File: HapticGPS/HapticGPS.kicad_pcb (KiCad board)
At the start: 4 copper layers, 35 x 50 mm, 106 parts, among them IC1 BOS1921CQR, J2 PZ, J3 Conn_01x02, J4 Conn_01x02, J5 Conn_01x10, Q1 RU1J002, U1 NPM1300, U2 NRF54L15-QFAA-R, U3 DRV2667RGPR, U4 CY15B108, U5 LC29H, U6 LSM6, U7 TPS22917DBV, Y1 32MHz, Y2 32kHz

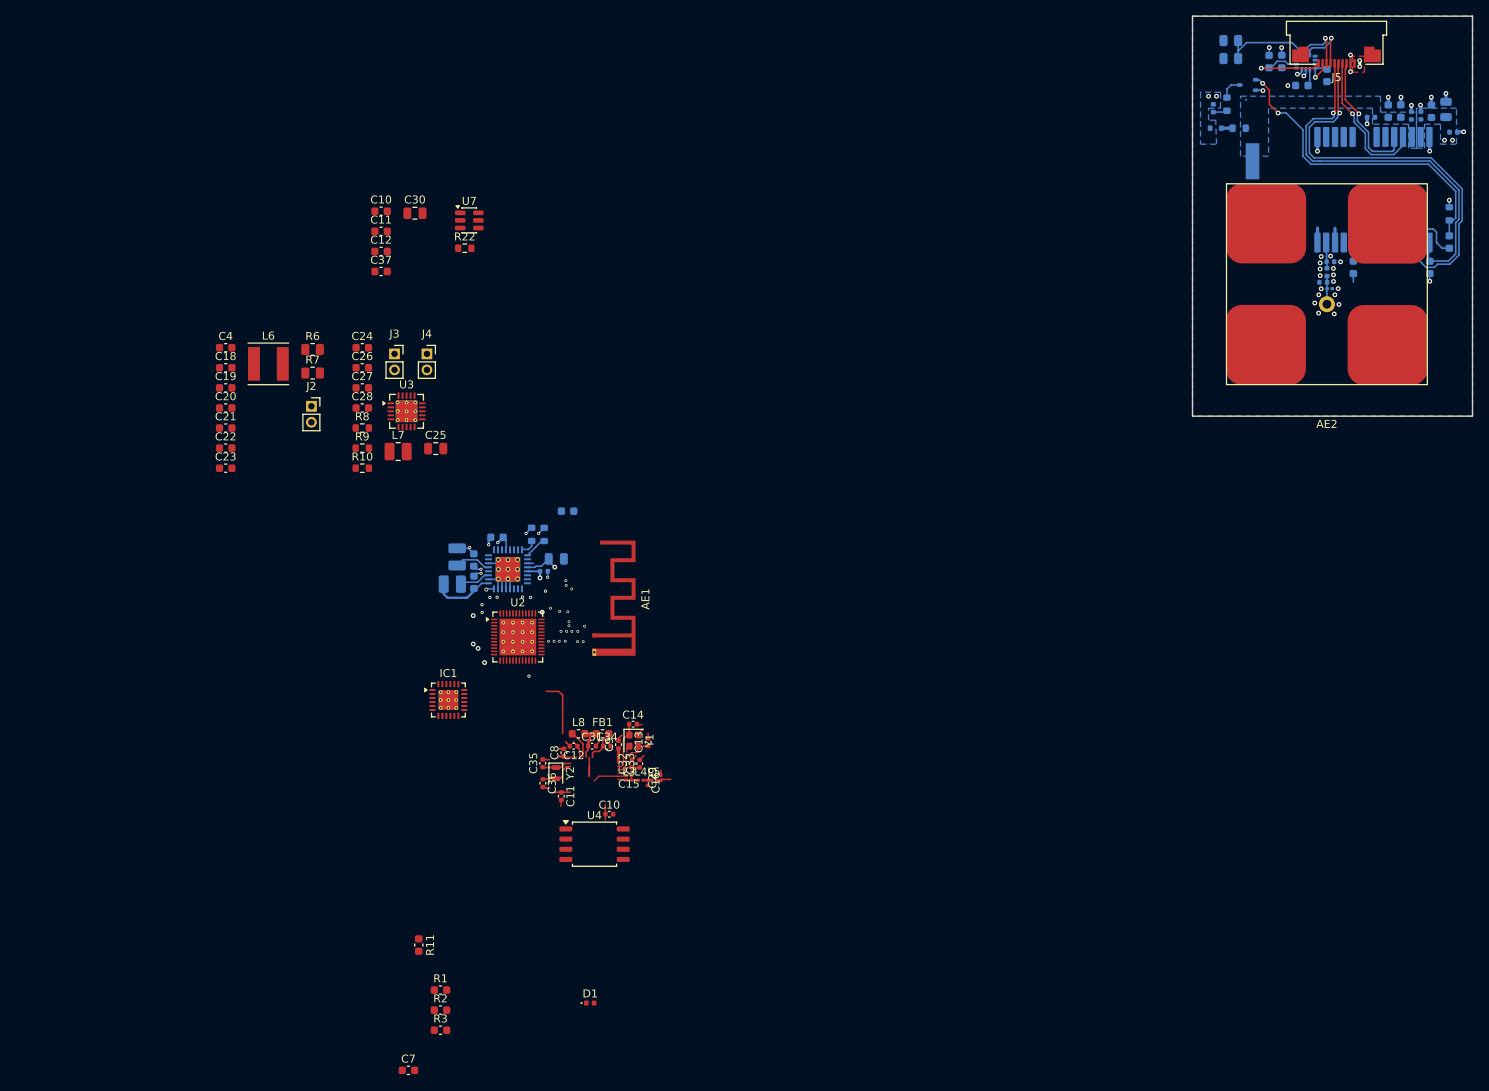
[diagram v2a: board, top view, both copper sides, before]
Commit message: eliminating GPS, and second piezo driver
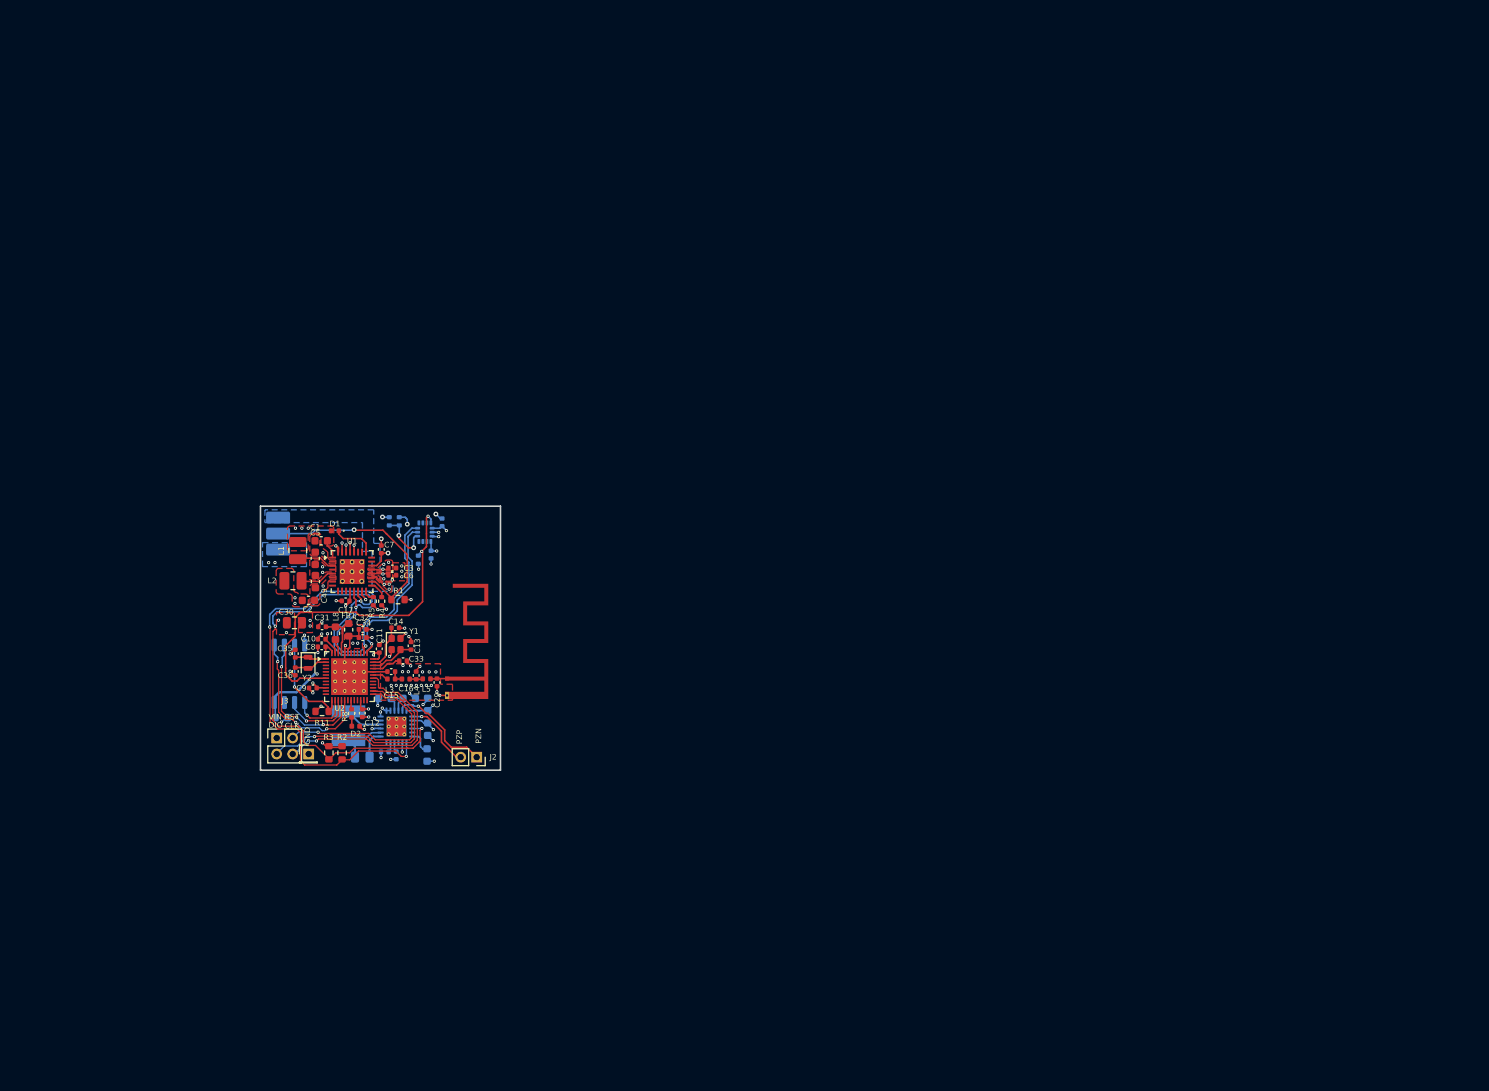
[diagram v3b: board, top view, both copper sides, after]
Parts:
- removed AE2: ANT-GNCP, Sadman_antenna:NT-GNCP-TH258L15
- removed the C10 at (174.1, 137.2)
- removed the C10 at (145.6, 61.9)
- removed the C11 at (145.6, 64.4)
- removed the C11 at (168.1, 135.0)
- removed the C12 at (169.7, 128.8)
- removed the C12 at (145.6, 66.9)
- removed C18, C27, C4, C42, C47, C48: 100nF, Capacitor_SMD:C_0603_1608Metric
- removed C24: 1uF, Capacitor_SMD:C_0603_1608Metric
- removed C25: 10uF, Capacitor_SMD:C_0805_2012Metric
- removed C40, C43: 33pF, Capacitor_SMD:C_0402_1005Metric
- removed C41: 4.7uF, Capacitor_SMD:C_0603_1608Metric
- removed C44: 220mF, sadman_power_passive:FC0H224ZFTBR24
- removed C45, C46: 2pF, Capacitor_SMD:C_0402_1005Metric
- removed D3: TVS, Diode_SMD:D_0402_1005Metric
- removed D4: 1N4148WT, Diode_SMD:D_SOD-523
- removed D5: TVS, Diode_SMD:D_0201_0603Metric
- removed D6: YELLOW, Diode_SMD:D_0402_1005Metric
- removed J5: Conn_01x10, Connector_FFC-FPC:Amphenol_F32Q-1A7x1-11010_1x10-1MP_P0.5mm_Horizontal
- removed L7: 2.2uF, Inductor_SMD:L_1008_2520Metric
- removed L9: 6nH, Inductor_SMD:L_0402_1005Metric
- removed Q1: RU1J002, Package_TO_SOT_SMD:SOT-323_SC-70
- removed R10: 7.68K, Resistor_SMD:R_0603_1608Metric
- removed R12, R22: 1k, Resistor_SMD:R_0603_1608Metric
- removed R13: 1, Resistor_SMD:R_0805_2012Metric
- removed R14, R17, R18, R20: 2.2k, Capacitor_SMD:C_0603_1608Metric
- removed R15: 100K, Resistor_SMD:R_0603_1608Metric
- removed R16: 75, Resistor_SMD:R_0603_1608Metric
- removed R9: 37k, Resistor_SMD:R_0603_1608Metric
- removed U3: DRV2667RGPR, Package_DFN_QFN:Texas_RGP0020D_VQFN-20-1EP_4x4mm_P0.5mm_EP2.7x2.7mm_ThermalVias
- removed U5: LC29H, Sadman_RF_receivers:LC29H
- removed U7: TPS22917DBV, Package_TO_SOT_SMD:SOT-23-6
- added C10: 100nF, Capacitor_SMD:C_0402_1005Metric, F.Cu at (138.1, 115.4)
- added C11: 100nF, Capacitor_SMD:C_0402_1005Metric, F.Cu at (145.3, 116.6)
- added C12: 100nF, Capacitor_SMD:C_0402_1005Metric, F.Cu at (143.2, 124.6)
- added C49: 10uF, Capacitor_SMD:C_0603_1608Metric, F.Cu at (137.4, 108.2)
- added J1: Conn_01x01, Connector_PinHeader_2.00mm:PinHeader_1x01_P2.00mm_Vertical, F.Cu at (136.5, 129.7)
- C1, C2, C3, U1: moved to F.Cu
- C15, C16, C29: footprint Capacitor_SMD:C_0201_0603Metric -> Capacitor_SMD:C_0402_1005Metric
- C17, C6: footprint Capacitor_SMD:C_0603_1608Metric -> Capacitor_SMD:C_0402_1005Metric; moved to F.Cu
- C19, C20, C21, C22, C23, C37, IC1, L6, R6, U4: moved to B.Cu
- C26, C28: footprint Capacitor_SMD:C_0603_1608Metric -> Capacitor_SMD:C_0402_1005Metric; moved to B.Cu
- C38: value 10uF -> 100nF; footprint Capacitor_SMD:C_0805_2012Metric -> Capacitor_SMD:C_0402_1005Metric
- C39, C7: footprint Capacitor_SMD:C_0603_1608Metric -> Capacitor_SMD:C_0402_1005Metric
- C5: footprint Capacitor_SMD:C_0805_2012Metric -> Capacitor_SMD:C_0603_1608Metric; moved to F.Cu
- D2: value TVS -> GREEN; footprint Diode_SMD:D_0402_1005Metric -> LED_SMD:LED_0402_1005Metric; moved to F.Cu
- J3: value Conn_01x02 -> Conn_02x02_Counter_Clockwise; footprint Connector_PinSocket_2.00mm:PinSocket_1x02_P2.00mm_Vertical -> Connector_PinHeader_2.00mm:PinHeader_2x02_P2.00mm_Vertical
- J4: value Conn_01x02 -> Conn_01x03; footprint Connector_PinSocket_2.00mm:PinSocket_1x02_P2.00mm_Vertical -> Solderpads:01x03_1.5x3; moved to B.Cu
- L1, L2: value 2.2uF -> 2.2uH; moved to F.Cu
- L3, L4, L5: footprint Inductor_SMD:L_0201_0603Metric -> Inductor_SMD:L_0402_1005Metric
- R1, R11, R2, R3: footprint Capacitor_SMD:C_0603_1608Metric -> Resistor_SMD:R_0603_1608Metric
- R19: footprint Resistor_SMD:R_0805_2012Metric -> Resistor_SMD:R_0402_1005Metric
- R21: value 2.2k -> 10k; footprint Capacitor_SMD:C_0603_1608Metric -> Resistor_SMD:R_0402_1005Metric
- R4: value 100K -> 300K; footprint Resistor_SMD:R_0603_1608Metric -> Resistor_SMD:R_0402_1005Metric; moved to F.Cu
- R5: value 100K -> 150K; footprint Resistor_SMD:R_0603_1608Metric -> Resistor_SMD:R_0402_1005Metric; moved to F.Cu
- R7: footprint Resistor_SMD:R_0805_2012Metric -> Resistor_SMD:R_0402_1005Metric; moved to B.Cu
- R8: value 510k -> 120; footprint Resistor_SMD:R_0603_1608Metric -> Resistor_SMD:R_0402_1005Metric
- Y2: value 32kHz -> 32.768kHz
- moved D2 156.0 mm to (142.4, 126.2), turned to 180 degrees
- moved C39 136.8 mm to (151.8, 104.8), turned to -90 degrees
- moved C38 135.7 mm to (153.2, 100.8)
- moved R21 128.7 mm to (150.2, 105.4)
- moved U6 124.8 mm to (151.0, 102.0), turned to -90 degrees
- moved R19 120.0 mm to (146.6, 100.6), turned to -90 degrees
- moved D1 67.1 mm to (139.8, 101.8), turned to 180 degrees
- moved C7 65.2 mm to (145.6, 104.2), turned to 90 degrees
- moved C37 57.1 mm to (133.1, 125.2)
- moved C30 53.4 mm to (134.7, 113.3), turned to 180 degrees
- moved C19 52.3 mm to (151.3, 129.8), turned to -90 degrees
- moved R6 51.3 mm to (143.2, 130.1)
- moved J3 50.2 mm to (132.5, 127.7)
- moved R1 49.1 mm to (147.7, 110.4)
- moved C26 48.6 mm to (147.5, 129.9), turned to -90 degrees
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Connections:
- net Net-(U1-PVDD) renamed /POWER/PVDD
- AE1 pad 2: (no net) -> GND
- C17 pad 1: +3VDC1 -> +3VDC2
- C22 pad 2: /PIEZOELECTRIC DRIVER/PZ_VDD_F -> +3VDC2
- C23 pad 2: /PIEZOELECTRIC DRIVER/PZ_VDD_F -> +3VDC2
- C26 pad 1: Net-(U3-VREG) -> Net-(IC1-REG)
- C28 pad 1: Net-(U3-VPUMP) -> Net-(IC1-PUMP)
- C37 pad 1: Net-(U4-VDD) -> +3VDC1
- C38 pad 1: /VINC_GPS -> +3VDC1
- C39 pad 1: /VINC_GPS -> +3VDC1
- D1 pad 2: GND -> +3VDC1
- D2 pad 1: /VINC_GPS -> GND
- D2 pad 2: GND -> Net-(D2-A)
- IC1 pad 2: /PIEZOELECTRIC DRIVER/PZ_VDD_F -> +3VDC2
- IC1 pad 24: /PIEZOELECTRIC DRIVER/PZ_VDD_F -> +3VDC2
- J3 pad 1: /PIEZOELECTRIC DRIVER 2/PZ2_OUT+ -> +5V
- J3 pad 2: /PIEZOELECTRIC DRIVER 2/PZ2_OUT- -> /CONTROLLER/NRF_RESET
- J4 pad 1: /PIEZOELECTRIC DRIVER 2/PZ2_IN+ -> GND
- J4 pad 2: /PIEZOELECTRIC DRIVER 2/PZ2_IN- -> /POWER/VBAT_NTC
- R2 pad 1: +2V8 -> +3VDC1
- R3 pad 1: +2V8 -> +3VDC1
- R7 pad 1: +3VDC2 -> +3VDC1
- R7 pad 2: /PIEZOELECTRIC DRIVER/PZ_VDD_F -> Net-(U6-CS)
- R8 pad 1: Net-(U3-PVDD) -> Net-(D2-A)
- R8 pad 2: Net-(U3-FB) -> Net-(U2-P2.08/TRACEDATA(1))
- U1 pad 12: +3VDC1 -> +3VDC2
- U2 pad 13: unconnected-(U2-P2.02-Pad13) -> /CONTROLLER/NRF_WPMEMORY
- U2 pad 14: unconnected-(U2-P2.03-Pad14) -> /CONTROLLER/NRF_MOSI
- U2 pad 15: unconnected-(U2-P2.04-Pad15) -> /CONTROLLER/NRF_SCK
- U2 pad 16: unconnected-(U2-P2.05-Pad16) -> /CONTROLLER/NRF_MISO
- U2 pad 17: unconnected-(U2-P2.06/TRACECLK-Pad17) -> /CONTROLLER/NRF_CSMEMORY
- U2 pad 19: unconnected-(U2-P2.08/TRACEDATA(1)-Pad19) -> Net-(U2-P2.08/TRACEDATA(1))
- U2 pad 37: unconnected-(U2-P1.09/ASO(2)/RADIO(0)-Pad37) -> /SCL
- U2 pad 38: unconnected-(U2-P1.10/ASI(2)/RADIO(1)-Pad38) -> /SDA
- U2 pad 7: unconnected-(U2-P1.06/ASO(1)/AIN2-Pad7) -> /IMU_INT1
- U4 pad 8: Net-(U4-VDD) -> +3VDC1
- U6 pad 13: /SCL_OUT -> /SCL
- U6 pad 14: /SDA_OUT -> /SDA
- U6 pad 5: /VINC_GPS -> +3VDC1
- U6 pad 8: /VINC_GPS -> +3VDC1
- U6 pad 9: /IMU_INT2 -> unconnected-(U6-INT2-Pad9)
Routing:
- net /SCL: track 0.00 -> 89.1 mm, vias 0 -> 4
- net /SDA: track 0.00 -> 88.4 mm, vias 0 -> 4
- net /GPS_NRST: track 60.4 -> 0.00 mm, vias 1 -> 0
- net /GPS_WK: track 49.9 -> 0.00 mm, vias 1 -> 0
- net Net-(Q1-G): track 39.8 -> 0.00 mm, vias 2 -> 0
- net /IMU_INT1: track 4.81 -> 43.0 mm, vias 1 -> 2
- net /CONTROLLER/NRF_SWDIO: track 0.00 -> 28.1 mm, vias 0 -> 1
- net /CONTROLLER/NRF_SWDCLK: track 0.00 -> 28.0 mm, vias 0 -> 1
- net /POWER/VBAT_NTC: track 0.00 -> 27.6 mm, vias 0 -> 1
- net /CONTROLLER/NRF_RESET: track 0.00 -> 24.6 mm, vias 0 -> 1
- net /CONTROLLER/NRF_CSMEMORY: track 0.00 -> 20.8 mm, vias 0 -> 3
- net /CONTROLLER/NRF_MISO: track 0.00 -> 19.1 mm, vias 0 -> 3
- net /GPS_TX: track 18.4 -> 0.00 mm, vias 1 -> 0
- net +3VDC2: track 10.4 -> 28.6 mm, vias 2 -> 7
- net /GPS_RX: track 17.0 -> 0.00 mm, vias 1 -> 0
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- added copper zone on F.Cu, net +3VDC1
- added copper zone on In2.Cu, net +3VDC1
- added copper zone on F.Cu, net +3VDC2
- added copper zone on In2.Cu, net +3VDC2
- added copper zone on F.Cu, net +5V
- added copper zone on In2.Cu, net +5V
- added copper zone on F.Cu, net /CONTROLLER/NRF_DECA
- added copper zone on In1.Cu, net /CONTROLLER/NRF_DECA
- added copper zone on F.Cu, net /POWER/PVDD
- added copper zone on In2.Cu, net /POWER/PVDD
- added copper zone on B.Cu, net /POWER/VBAT
- added copper zone on F.Cu, net /POWER/VBAT
- removed copper zone on B.Cu, net /GPS_INTERFACE/VBACKUP_GPS
- removed copper zone on B.Cu, net /VINC_GPS
- removed copper zone on F.Cu, net /VINC_GPS
- removed copper zone on In2.Cu, net /VINC_GPS
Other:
- board size 35 x 50 mm -> 30 x 33 mm
- board text added: "0"
- board text added: "0 mm"
- board text added: "0.01 mm"
- board text added: "0.0175 mm"
- board text added: "0.02"
- board text added: "0.035 mm"
- board text added: "0.1500 mm / 0.1200 mm"
- board text added: "0.1855 mm"
- board text added: "0.2000 mm"
- board text added: "1"
- board text added: "1.03 mm"
- board text added: "1.5260 mm"
- board text added: "3.3"
- board text added: "30.0000 mm x 33.0000 mm"
- board text added: "4"
- board text added: "4.5"
- board text added: "50 OHMS"
- board text added: "B.Cu"
- board text added: "B.Mask"
- board text added: "B.Paste"
- board text added: "B.Silkscreen"
- board text added: "BOARD CHARACTERISTICS"
- board text added: "Board Thickness:"
- board text added: "Board overall dimensions:"
- board text added: "Bottom Silk Screen"
- board text added: "Bottom Solder Mask"
- board text added: "Bottom Solder Paste"
- board text added: "CLK"
- board text added: "Castellated pads:"
- board text added: "Color"
- board text added: "Copper Finish:"
- board text added: "Copper Layer Count:"
- board text added: "DIO"
- board text added: "Dielectric 1"
- board text added: "Dielectric 2"
- board text added: "Dielectric 3"
- board text added: "Direct Printing"
- board text added: "Edge card connectors:"
- board text added: "Epsilon R"
- board text added: "F.Cu"
- board text added: "F.Mask"
- board text added: "F.Paste"
- board text added: "F.Silkscreen"
- board text added: "FR4"
- board text added: "GND"
- board text added: "Green"
- board text added: "Impedance Control:"
- board text added: "In1.Cu"
- board text added: "In2.Cu"
- board text added: "Layer Name"
- board text added: "Liquid Ink"
- board text added: "Loss Tangent"
- board text added: "Material"
- board text added: "Min hole diameter:"
- board text added: "Min track/spacing:"
- board text added: "NTC"
- board text added: "No"
- board text added: "None"
- board text added: "Not specified"
- board text added: "PZN"
- board text added: "PZP"
- board text added: "Plated Board Edge:"
- board text added: "RST"
- board text added: "Thickness (mm)"
- board text added: "Top Silk Screen"
- board text added: "Top Solder Mask"
- board text added: "Top Solder Paste"
- board text added: "Type"
- board text added: "VBAT"
- board text added: "VIN"
- board text added: "White"
- board text added: "Yes"
- board text added: "copper"
- board text added: "core"
- board text added: "prepreg"
